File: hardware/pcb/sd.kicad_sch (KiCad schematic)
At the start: 2 parts, among them J1 Micro_SD_Card_Det1, J2 Micro_SD_Card_Det1

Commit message: bunch of small changes
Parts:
- added C34, C35, C36: 22u, symbol Device:C_Small
- added R13, R14, R15, R16, R17, R19, R20, R21, R22, R23: 47k, symbol Device:R_Small
- added R18, R24: 10k, symbol Device:R_Small
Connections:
- net EXT.DAT2: now reaches J1.1 (DAT2)
- net EXT.DAT2: now also R19.2
- net EXT.DAT3: now reaches J1.2 (DAT3/CD)
- net EXT.DAT3: now also R20.2
- net EXT.CMD: now reaches J1.3 (CMD)
- net EXT.CMD: now also R21.2
- net +3V3: now reaches J1.4 (VDD)
- net +3V3: now also J2.4 (VDD), C34.1, C35.1, C36.1, R13.1, R14.1, R15.1, R16.1, R17.1, R18.1, R19.1, R20.1, R21.1, R22.1, R23.1, R24.1
- net EXT.CK: now reaches J1.5 (CLK)
- net GND: now reaches J1.6 (VSS)
- net GND: now also J1.SH (SHIELD), J2.6 (VSS), J2.SH (SHIELD), C34.2, C35.2, C36.2
- net EXT.DAT0: now reaches J1.7 (DAT0)
- net EXT.DAT0: now also R22.2
- net EXT.DAT1: now reaches J1.8 (DAT1)
- net EXT.DAT1: now also R23.2
- net EXT.CD: now reaches J1.9 (DET)
- net EXT.CD: now also R24.2
- net BOOT.DAT2: now reaches J2.1 (DAT2)
- net BOOT.DAT2: now also R13.2
- net BOOT.DAT3: now reaches J2.2 (DAT3/CD)
- net BOOT.DAT3: now also R14.2
- net BOOT.CMD: now reaches J2.3 (CMD)
- net BOOT.CMD: now also R15.2
- net BOOT.CK: now reaches J2.5 (CLK)
- net BOOT.DAT0: now reaches J2.7 (DAT0)
- net BOOT.DAT0: now also R16.2
- net BOOT.DAT1: now reaches J2.8 (DAT1)
- net BOOT.DAT1: now also R17.2
- net BOOT.CD: now reaches J2.9 (DET)
- net BOOT.CD: now also R18.2
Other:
- note added: "BOOT SD"
- note added: "EXTERNAl SD"
- note added: "Link: Altium SD card recommendations"
- note added: "No ESD protection added For first protype this is fine If needed I'll add later"
- note removed: "External storage"
- note removed: "OS storage"
- moved on the sheet: J1, J2

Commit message: small changes
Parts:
- C34: value 22u -> 10u
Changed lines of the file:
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@@
 			)
 		)
-		(property "Value" "22u"
+		(property "Value" "10u"
 			(at 155.448 56.642 0)
 			(show_name no)

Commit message: moved stuff around
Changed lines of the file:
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@@
 	)
 	(hierarchical_label "EXT{SDMMC}"
-		(shape input)
+		(shape bidirectional)
 		(at 40.64 114.3 180)
 		(effects
@@
 	)
 	(hierarchical_label "BOOT{SDMMC}"
-		(shape input)
+		(shape bidirectional)
 		(at 40.64 45.72 180)
 		(effects

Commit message: looking over stuff, added caps
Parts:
- C34: footprint (none) -> Capacitor_SMD:C_0402_1005Metric
- C35, C36: footprint (none) -> Capacitor_SMD:C_0603_1608Metric
- R13, R14, R15, R16, R17, R18, R19, R20, R21, R22, R23, R24: footprint (none) -> Resistor_SMD:R_0402_1005Metric
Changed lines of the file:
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@@
 			)
 		)
-		(property "Footprint" ""
+		(property "Footprint" "Resistor_SMD:R_0402_1005Metric"
 			(at 83.82 36.83 0)
 			(hide yes)
@@
 			)
 		)
-		(property "Footprint" ""
+		(property "Footprint" "Resistor_SMD:R_0402_1005Metric"
 			(at 58.42 36.83 0)
 			(hide yes)
@@
 			)
 		)
-		(property "Footprint" ""
+		(property "Footprint" "Capacitor_SMD:C_0603_1608Metric"
 			(at 153.67 124.46 0)
 			(hide yes)
@@
 			)
 		)
-		(property "Footprint" ""
+		(property "Footprint" "Resistor_SMD:R_0402_1005Metric"
 			(at 58.42 105.41 0)
 			(hide yes)
@@
 			)
 		)
-		(property "Footprint" ""
+		(property "Footprint" "Resistor_SMD:R_0402_1005Metric"
 			(at 77.47 105.41 0)
 			(hide yes)
@@
 			)
 		)
-		(property "Footprint" ""
+		(property "Footprint" "Resistor_SMD:R_0402_1005Metric"
 			(at 83.82 105.41 0)
 			(hide yes)
@@
 			)
 		)
-		(property "Footprint" ""
+		(property "Footprint" "Resistor_SMD:R_0402_1005Metric"
 			(at 90.17 36.83 0)
 			(hide yes)
@@
 			)
 		)
-		(property "Footprint" ""
+		(property "Footprint" "Resistor_SMD:R_0402_1005Metric"
 			(at 64.77 105.41 0)
 			(hide yes)
@@
 			)
 		)
-		(property "Footprint" ""
+		(property "Footprint" "Resistor_SMD:R_0402_1005Metric"
 			(at 71.12 105.41 0)
 			(hide yes)
@@
 			)
 		)
-		(property "Footprint" ""
+		(property "Footprint" "Capacitor_SMD:C_0402_1005Metric"
 			(at 153.67 55.88 0)
 			(hide yes)
@@
 			)
 		)
-		(property "Footprint" ""
+		(property "Footprint" "Resistor_SMD:R_0402_1005Metric"
 			(at 64.77 36.83 0)
 			(hide yes)
@@
 			)
 		)
-		(property "Footprint" ""
+		(property "Footprint" "Resistor_SMD:R_0402_1005Metric"
 			(at 71.12 36.83 0)
 			(hide yes)
@@
 			)
 		)
-		(property "Footprint" ""
+		(property "Footprint" "Capacitor_SMD:C_0603_1608Metric"
 			(at 161.29 124.46 0)
 			(hide yes)
@@
 			)
 		)
-		(property "Footprint" ""
+		(property "Footprint" "Resistor_SMD:R_0402_1005Metric"
 			(at 77.47 36.83 0)
 			(hide yes)
@@
 			)
 		)
-		(property "Footprint" ""
+		(property "Footprint" "Resistor_SMD:R_0402_1005Metric"
 			(at 90.17 105.41 0)
 			(hide yes)

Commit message: started cleaning up schematic
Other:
- company: (none) -> Gensis
- title: (none) -> SD Cards
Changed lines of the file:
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@@
 	(generator_version "10.0")
 	(paper "A4")
+	(title_block
+		(title "SD Cards")
+		(rev "v1.0.0")
+		(company "Gensis")
+	)
 	(rectangle
 		(start 22.86 21.59)

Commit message: mainboard: adde notes
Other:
- note added: "No ESD protection added For first protype this is fine Will be added later"
- note removed: "No ESD protection added For first protype this is fine If needed I'll add later"
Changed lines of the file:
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@@
 		)
 	)
-	(text "No ESD protection added\nFor first protype this is fine\nIf needed I'll add later"
+	(text "No ESD protection added\nFor first protype this is fine\nWill be added later"
 		(exclude_from_sim no)
 		(at 175.26 88.392 0)

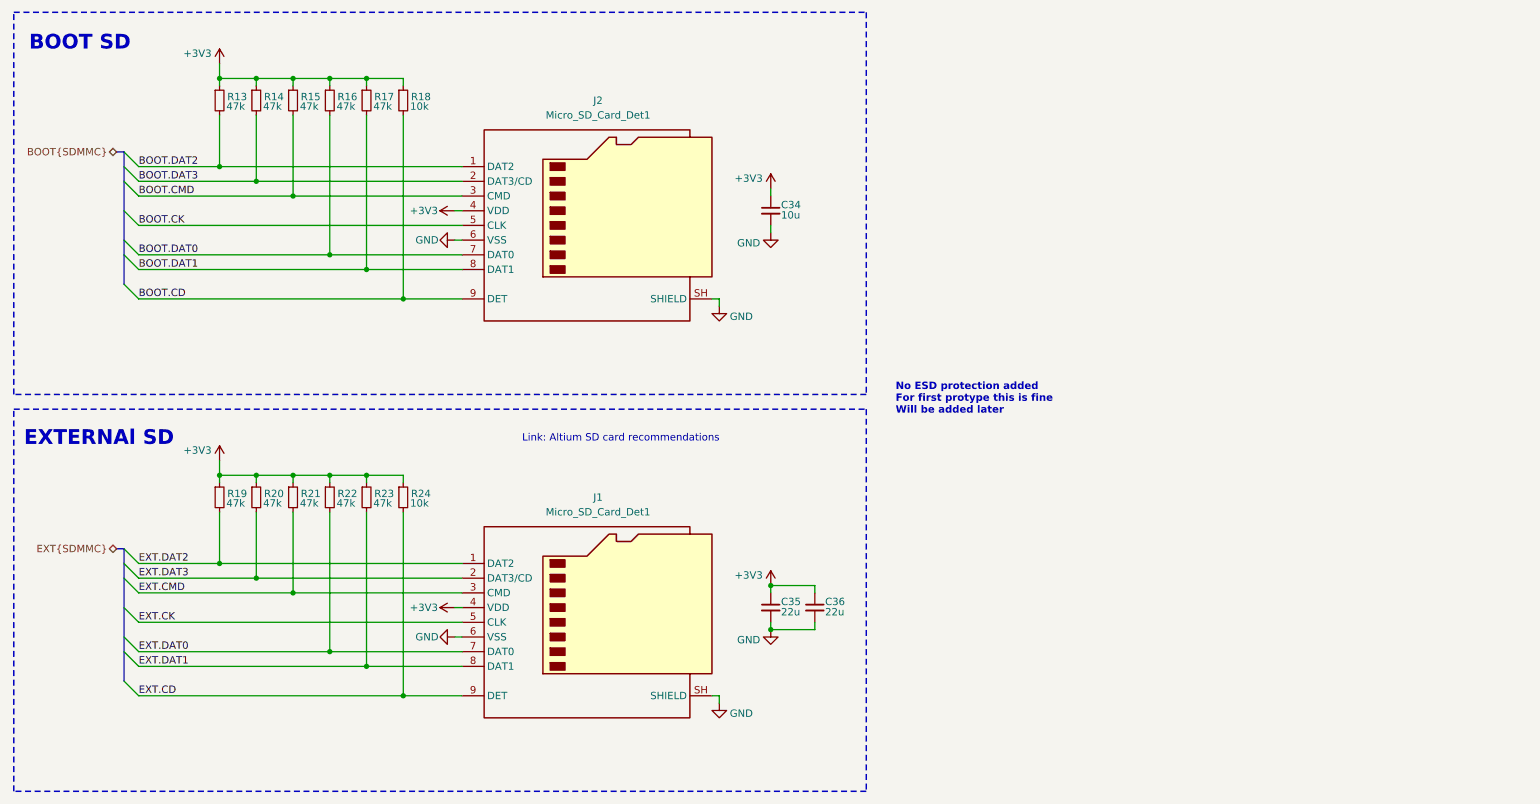
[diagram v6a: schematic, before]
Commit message: mainboard: reannotated schematic
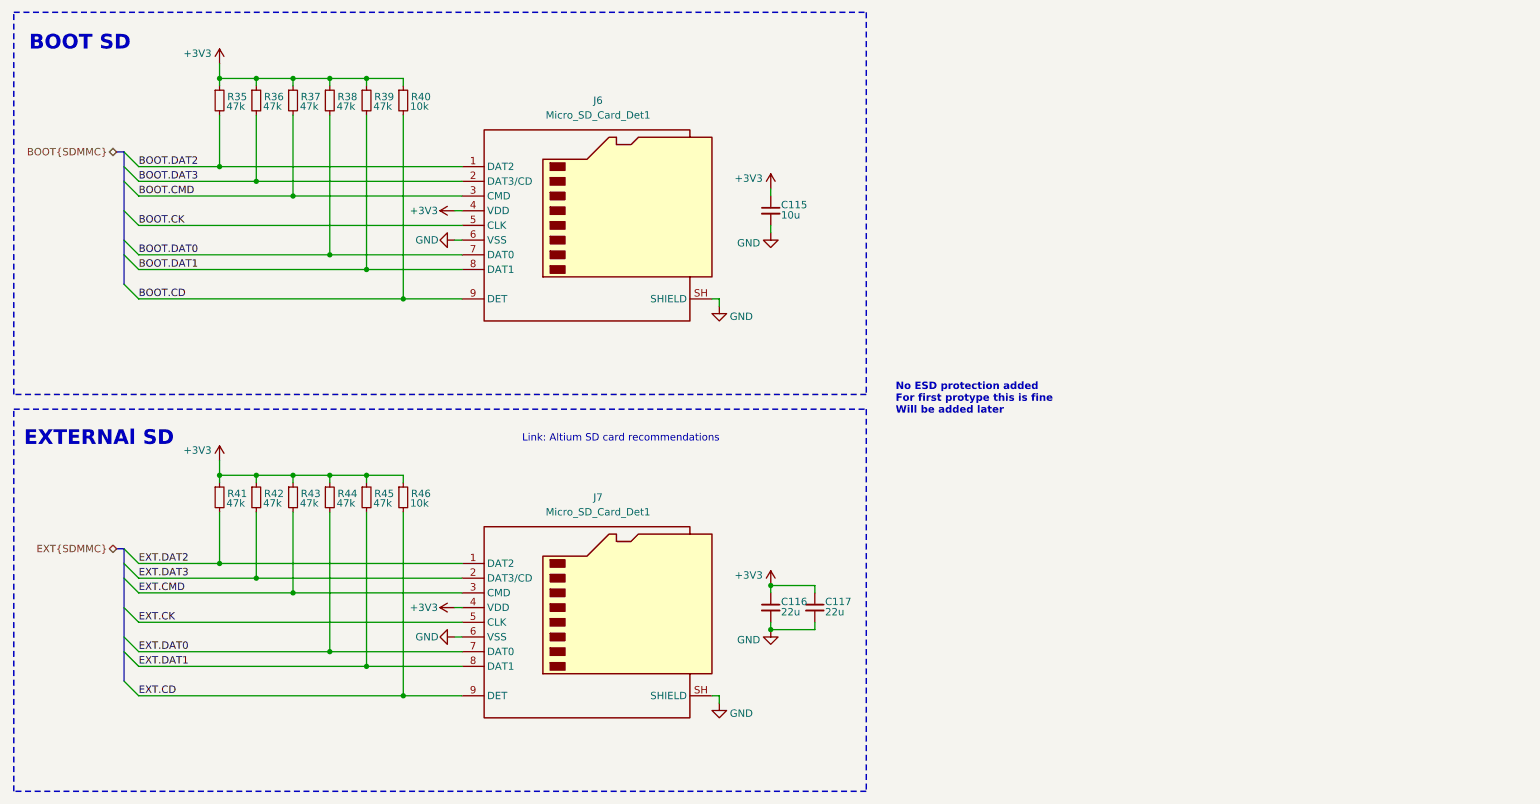
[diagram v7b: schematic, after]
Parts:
- renumbered C34 to C115, C35 to C116, C36 to C117, J2 to J6, J1 to J7, R13 to R35, R14 to R36, R15 to R37, R16 to R38, R17 to R39, R18 to R40, R19 to R41, R20 to R42, R21 to R43, R22 to R44, R23 to R45, R24 to R46
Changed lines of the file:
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@@
 		(in_pos_files yes)
 		(dnp no)
-		(property "Reference" "R17"
+		(property "Reference" "R39"
 			(at 86.868 36.195 0)
 			(show_name no)
@@
 			(project "meko"
 				(path "/da54f10a-146b-4941-a9c7-55c7173bb101/45aa24d2-e0af-4ebb-a68a-61b6a12c0eec"
-					(reference "R17")
+					(reference "R39")
 					(unit 1)
 				)
@@
 		(in_pos_files yes)
 		(dnp no)
-		(property "Reference" "R13"
+		(property "Reference" "R35"
 			(at 61.468 36.195 0)
 			(show_name no)
@@
 			(project "meko"
 				(path "/da54f10a-146b-4941-a9c7-55c7173bb101/45aa24d2-e0af-4ebb-a68a-61b6a12c0eec"
-					(reference "R13")
+					(reference "R35")
 					(unit 1)
 				)
@@
 		(in_pos_files yes)
 		(dnp no)
-		(property "Reference" "#PWR070"
+		(property "Reference" "#PWR0116"
 			(at 102.87 55.88 0)
 			(hide yes)
@@
 			(project "meko"
 				(path "/da54f10a-146b-4941-a9c7-55c7173bb101/45aa24d2-e0af-4ebb-a68a-61b6a12c0eec"
-					(reference "#PWR070")
+					(reference "#PWR0116")
 					(unit 1)
 				)
@@
 		(in_pos_files yes)
 		(dnp no)
-		(property "Reference" "C35"
+		(property "Reference" "C116"
 			(at 155.448 123.444 0)
 			(show_name no)
@@
 			(project "meko"
 				(path "/da54f10a-146b-4941-a9c7-55c7173bb101/45aa24d2-e0af-4ebb-a68a-61b6a12c0eec"
-					(reference "C35")
+					(reference "C116")
 					(unit 1)
 				)
@@
 		(dnp no)
 		(fields_autoplaced yes)
-		(property "Reference" "J1"
+		(property "Reference" "J7"
 			(at 123.825 105.41 0)
 			(show_name no)
@@
 			(project "meko"
 				(path "/da54f10a-146b-4941-a9c7-55c7173bb101/45aa24d2-e0af-4ebb-a68a-61b6a12c0eec"
-					(reference "J1")
+					(reference "J7")
 					(unit 1)
 				)
@@
 		(in_pos_files yes)
 		(dnp no)
-		(property "Reference" "R19"
+		(property "Reference" "R41"
 			(at 61.468 104.775 0)
 			(show_name no)
@@
 			(project "meko"
 				(path "/da54f10a-146b-4941-a9c7-55c7173bb101/45aa24d2-e0af-4ebb-a68a-61b6a12c0eec"
-					(reference "R19")
+					(reference "R41")
 					(unit 1)
 				)
@@
 		(in_pos_files yes)
 		(dnp no)
-		(property "Reference" "#PWR083"
+		(property "Reference" "#PWR0123"
 			(at 153.67 134.62 0)
 			(hide yes)
@@
 			(project "meko"
 				(path "/da54f10a-146b-4941-a9c7-55c7173bb101/45aa24d2-e0af-4ebb-a68a-61b6a12c0eec"
-					(reference "#PWR083")
+					(reference "#PWR0123")
 					(unit 1)
 				)
@@
 		(dnp no)
 		(fields_autoplaced yes)
-		(property "Reference" "J2"
+		(property "Reference" "J6"
 			(at 123.825 36.83 0)
 			(show_name no)
@@
 			(project "meko"
 				(path "/da54f10a-146b-4941-a9c7-55c7173bb101/45aa24d2-e0af-4ebb-a68a-61b6a12c0eec"
-					(reference "J2")
+					(reference "J6")
 					(unit 1)
 				)
@@
 		(in_pos_files yes)
 		(dnp no)
-		(property "Reference" "R22"
+		(property "Reference" "R44"
 			(at 80.518 104.775 0)
 			(show_name no)
@@
 			(project "meko"
 				(path "/da54f10a-146b-4941-a9c7-55c7173bb101/45aa24d2-e0af-4ebb-a68a-61b6a12c0eec"
-					(reference "R22")
+					(reference "R44")
 					(unit 1)
 				)
@@
 		(in_pos_files yes)
 		(dnp no)
-		(property "Reference" "#PWR072"
+		(property "Reference" "#PWR0114"
 			(at 58.42 34.29 0)
 			(hide yes)
@@
 			(project "meko"
 				(path "/da54f10a-146b-4941-a9c7-55c7173bb101/45aa24d2-e0af-4ebb-a68a-61b6a12c0eec"
-					(reference "#PWR072")
+					(reference "#PWR0114")
 					(unit 1)
 				)
@@
 		(in_pos_files yes)
 		(dnp no)
-		(property "Reference" "R23"
+		(property "Reference" "R45"
 			(at 86.868 104.775 0)
 			(show_name no)
@@
 			(project "meko"
 				(path "/da54f10a-146b-4941-a9c7-55c7173bb101/45aa24d2-e0af-4ebb-a68a-61b6a12c0eec"
-					(reference "R23")
+					(reference "R45")
 					(unit 1)
 				)
@@
 		(in_pos_files yes)
 		(dnp no)
-		(property "Reference" "R18"
+		(property "Reference" "R40"
 			(at 93.218 36.195 0)
 			(show_name no)
@@
 			(project "meko"
 				(path "/da54f10a-146b-4941-a9c7-55c7173bb101/45aa24d2-e0af-4ebb-a68a-61b6a12c0eec"
-					(reference "R18")
+					(reference "R40")
 					(unit 1)
 				)
@@
 		(in_pos_files yes)
 		(dnp no)
-		(property "Reference" "R20"
+		(property "Reference" "R42"
 			(at 67.818 104.775 0)
 			(show_name no)
@@
 			(project "meko"
 				(path "/da54f10a-146b-4941-a9c7-55c7173bb101/45aa24d2-e0af-4ebb-a68a-61b6a12c0eec"
-					(reference "R20")
+					(reference "R42")
 					(unit 1)
 				)
@@
 		(in_pos_files yes)
 		(dnp no)
-		(property "Reference" "R21"
+		(property "Reference" "R43"
 			(at 74.168 104.775 0)
 			(show_name no)
@@
 			(project "meko"
 				(path "/da54f10a-146b-4941-a9c7-55c7173bb101/45aa24d2-e0af-4ebb-a68a-61b6a12c0eec"
-					(reference "R21")
+					(reference "R43")
 					(unit 1)
 				)
@@
 		(in_pos_files yes)
 		(dnp no)
-		(property "Reference" "C34"
+		(property "Reference" "C115"
 			(at 155.448 54.864 0)
 			(show_name no)
@@
 			(project "meko"
 				(path "/da54f10a-146b-4941-a9c7-55c7173bb101/45aa24d2-e0af-4ebb-a68a-61b6a12c0eec"
-					(reference "C34")
+					(reference "C115")
 					(unit 1)
 				)
@@
 		(in_pos_files yes)
 		(dnp no)
-		(property "Reference" "#PWR079"
+		(property "Reference" "#PWR0122"
 			(at 102.87 124.46 0)
 			(hide yes)
@@
 			(project "meko"
 				(path "/da54f10a-146b-4941-a9c7-55c7173bb101/45aa24d2-e0af-4ebb-a68a-61b6a12c0eec"
-					(reference "#PWR079")
+					(reference "#PWR0122")
 					(unit 1)
 				)
@@
 		(in_pos_files yes)
 		(dnp no)
-		(property "Reference" "#PWR071"
+		(property "Reference" "#PWR0118"
 			(at 92.71 60.96 0)
 			(hide yes)
@@
 			(project "meko"
 				(path "/da54f10a-146b-4941-a9c7-55c7173bb101/45aa24d2-e0af-4ebb-a68a-61b6a12c0eec"
-					(reference "#PWR071")
+					(reference "#PWR0118")
 					(unit 1)
 				)
@@
 		(in_pos_files yes)
 		(dnp no)
-		(property "Reference" "#PWR082"
+		(property "Reference" "#PWR0121"
 			(at 153.67 124.46 0)
 			(hide yes)
@@
 			(project "meko"
 				(path "/da54f10a-146b-4941-a9c7-55c7173bb101/45aa24d2-e0af-4ebb-a68a-61b6a12c0eec"
-					(reference "#PWR082")
+					(reference "#PWR0121")
 					(unit 1)
 				)
@@
 		(in_pos_files yes)
 		(dnp no)
-		(property "Reference" "#PWR080"
+		(property "Reference" "#PWR0124"
 			(at 92.71 129.54 0)
 			(hide yes)
@@
 			(project "meko"
 				(path "/da54f10a-146b-4941-a9c7-55c7173bb101/45aa24d2-e0af-4ebb-a68a-61b6a12c0eec"
-					(reference "#PWR080")
+					(reference "#PWR0124")
 					(unit 1)
 				)
@@
 		(in_pos_files yes)
 		(dnp no)
-		(property "Reference" "#PWR075"
+		(property "Reference" "#PWR0119"
 			(at 144.78 78.74 0)
 			(hide yes)
@@
 			(project "meko"
 				(path "/da54f10a-146b-4941-a9c7-55c7173bb101/45aa24d2-e0af-4ebb-a68a-61b6a12c0eec"
-					(reference "#PWR075")
+					(reference "#PWR0119")
 					(unit 1)
 				)
@@
 		(in_pos_files yes)
 		(dnp no)
-		(property "Reference" "#PWR076"
+		(property "Reference" "#PWR0115"
 			(at 153.67 55.88 0)
 			(hide yes)
@@
 			(project "meko"
 				(path "/da54f10a-146b-4941-a9c7-55c7173bb101/45aa24d2-e0af-4ebb-a68a-61b6a12c0eec"
-					(reference "#PWR076")
+					(reference "#PWR0115")
 					(unit 1)
 				)
@@
 		(in_pos_files yes)
 		(dnp no)
-		(property "Reference" "#PWR077"
+		(property "Reference" "#PWR0117"
 			(at 153.67 66.04 0)
 			(hide yes)
@@
 			(project "meko"
 				(path "/da54f10a-146b-4941-a9c7-55c7173bb101/45aa24d2-e0af-4ebb-a68a-61b6a12c0eec"
-					(reference "#PWR077")
+					(reference "#PWR0117")
 					(unit 1)
 				)
@@
 		(in_pos_files yes)
 		(dnp no)
-		(property "Reference" "R14"
+		(property "Reference" "R36"
 			(at 67.818 36.195 0)
 			(show_name no)
@@
 			(project "meko"
 				(path "/da54f10a-146b-4941-a9c7-55c7173bb101/45aa24d2-e0af-4ebb-a68a-61b6a12c0eec"
-					(reference "R14")
+					(reference "R36")
 					(unit 1)
 				)
@@
 		(in_pos_files yes)
 		(dnp no)
-		(property "Reference" "R15"
+		(property "Reference" "R37"
 			(at 74.168 36.195 0)
 			(show_name no)
@@
 			(project "meko"
 				(path "/da54f10a-146b-4941-a9c7-55c7173bb101/45aa24d2-e0af-4ebb-a68a-61b6a12c0eec"
-					(reference "R15")
+					(reference "R37")
 					(unit 1)
 				)
@@
 		(in_pos_files yes)
 		(dnp no)
-		(property "Reference" "#PWR081"
+		(property "Reference" "#PWR0125"
 			(at 144.78 147.32 0)
 			(hide yes)
@@
 			(project "meko"
 				(path "/da54f10a-146b-4941-a9c7-55c7173bb101/45aa24d2-e0af-4ebb-a68a-61b6a12c0eec"
-					(reference "#PWR081")
+					(reference "#PWR0125")
 					(unit 1)
 				)
@@
 		(in_pos_files yes)
 		(dnp no)
-		(property "Reference" "C36"
+		(property "Reference" "C117"
 			(at 163.068 123.444 0)
 			(show_name no)
@@
 			(project "meko"
 				(path "/da54f10a-146b-4941-a9c7-55c7173bb101/45aa24d2-e0af-4ebb-a68a-61b6a12c0eec"
-					(reference "C36")
+					(reference "C117")
 					(unit 1)
 				)
@@
 		(in_pos_files yes)
 		(dnp no)
-		(property "Reference" "R16"
+		(property "Reference" "R38"
 			(at 80.518 36.195 0)
 			(show_name no)
@@
 			(project "meko"
 				(path "/da54f10a-146b-4941-a9c7-55c7173bb101/45aa24d2-e0af-4ebb-a68a-61b6a12c0eec"
-					(reference "R16")
+					(reference "R38")
 					(unit 1)
 				)
@@
 		(in_pos_files yes)
 		(dnp no)
-		(property "Reference" "R24"
+		(property "Reference" "R46"
 			(at 93.218 104.775 0)
 			(show_name no)
@@
 			(project "meko"
 				(path "/da54f10a-146b-4941-a9c7-55c7173bb101/45aa24d2-e0af-4ebb-a68a-61b6a12c0eec"
-					(reference "R24")
+					(reference "R46")
 					(unit 1)
 				)
@@
 		(in_pos_files yes)
 		(dnp no)
-		(property "Reference" "#PWR078"
+		(property "Reference" "#PWR0120"
 			(at 58.42 102.87 0)
 			(hide yes)
@@
 			(project "meko"
 				(path "/da54f10a-146b-4941-a9c7-55c7173bb101/45aa24d2-e0af-4ebb-a68a-61b6a12c0eec"
-					(reference "#PWR078")
-					(unit 1)
-				)
+					(reference "#PWR0120")
+					(unit 1)
+				)

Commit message: added a bunch testpoints
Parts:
- added TP60: BOOT_DAT2, TestPoint:TestPoint_Pad_D1.0mm, symbol Connector:TestPoint
- added TP61: BOOT_DAT3, TestPoint:TestPoint_Pad_D1.0mm, symbol Connector:TestPoint
- added TP62: BOOT_DAT0, TestPoint:TestPoint_Pad_D1.0mm, symbol Connector:TestPoint
- added TP63: BOOT_DAT1, TestPoint:TestPoint_Pad_D1.0mm, symbol Connector:TestPoint
- added TP64: BOOT_CMD, TestPoint:TestPoint_Pad_D1.0mm, symbol Connector:TestPoint
- added TP65: BOOT_CK, TestPoint:TestPoint_Pad_D1.0mm, symbol Connector:TestPoint
- added TP66: BOOT_CD, TestPoint:TestPoint_Pad_D1.0mm, symbol Connector:TestPoint
- added TP67: EXT_DAT2, TestPoint:TestPoint_Pad_D1.0mm, symbol Connector:TestPoint
- added TP68: EXT_DAT3, TestPoint:TestPoint_Pad_D1.0mm, symbol Connector:TestPoint
- added TP69: EXT_CMD, TestPoint:TestPoint_Pad_D1.0mm, symbol Connector:TestPoint
- added TP70: EXT_CK, TestPoint:TestPoint_Pad_D1.0mm, symbol Connector:TestPoint
- added TP71: EXT_DAT0, TestPoint:TestPoint_Pad_D1.0mm, symbol Connector:TestPoint
- added TP72: EXT_DAT1, TestPoint:TestPoint_Pad_D1.0mm, symbol Connector:TestPoint
- added TP73: EXT_CD, TestPoint:TestPoint_Pad_D1.0mm, symbol Connector:TestPoint
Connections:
- net BOOT.CD: now also TP66.1
- net BOOT.CK: now also TP65.1
- net BOOT.CMD: now also TP64.1
- net BOOT.DAT0: now also TP62.1
- net BOOT.DAT1: now also TP63.1
- net BOOT.DAT2: now also TP60.1
- net BOOT.DAT3: now also TP61.1
- net EXT.CD: now also TP73.1
- net EXT.CK: now also TP70.1
- net EXT.CMD: now also TP69.1
- net EXT.DAT0: now also TP71.1
- net EXT.DAT1: now also TP72.1
- net EXT.DAT2: now also TP67.1
- net EXT.DAT3: now also TP68.1
